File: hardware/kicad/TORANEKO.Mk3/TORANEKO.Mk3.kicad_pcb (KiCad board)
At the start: 2 copper layers, 47.4 x 64 mm, 93 parts, among them IC1 MP6551GQB-P, IC2 MP6551GQB-P, IC3 NCR321PASX, IC4 NCR321PASX, IC5 AS5047P-ATSM, IC6 STM32F411CEU6TR, IC7 AS5047P-ATSM, IC8 NCR321PASX, IC9 NCR321PASX, J1 Conn_01x02_Pin, J2 Conn_01x02_Pin, J3 Conn_01x02_Male, J4 Conn_01x02_Pin, J5 Conn_01x02_Pin, J6 Conn_02x03_Odd_Even, Q1 IRLML6402, Q5 IRLML6344, SW1 SW_Push, U1 LSM6DSRXTR, U2 LXDC55FAAA-203, U3 Encord, U4 Encord_B, U5 Encord, U6 Encord_B, Y1 CSTNE10M0G52Z000R0

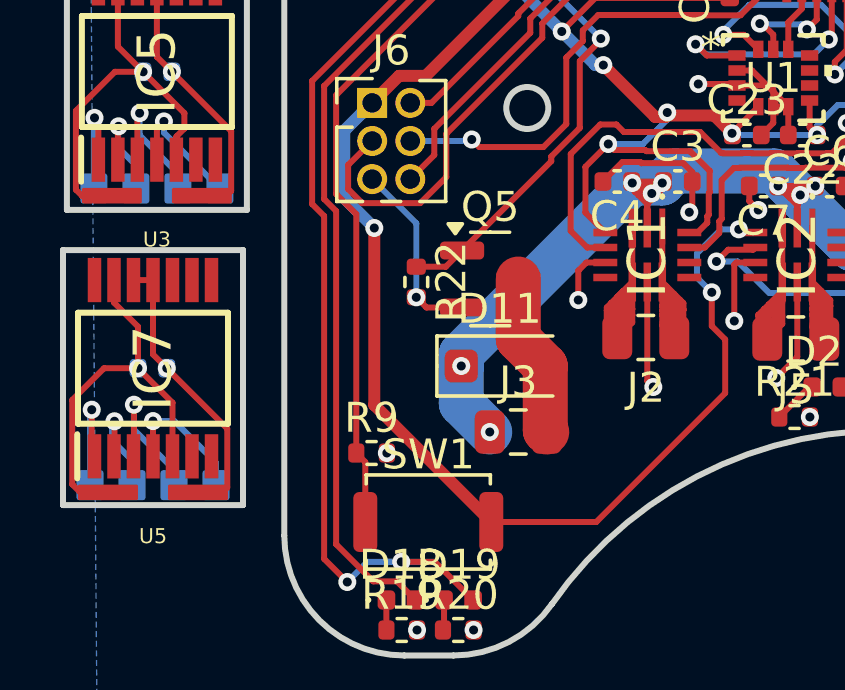
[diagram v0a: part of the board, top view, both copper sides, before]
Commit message: Main PCB check fixes: encoder B edge gap, via spacing, fine-pitch DRC rule
- Move encoder board B outline down 0.05mm so U5 pads are 0.213mm from
  the edge (same as U3; was 0.163mm). Panel regenerated to match.
- Nudge VBAT via at (102.15, 82.65) to (102.1, 82.7): hole gap 0.195 -> 0.27mm
- Add TORANEKO.Mk3.kicad_dru allowing 0.14mm between pads of U1 (LGA-14)
  and IC6 (UFQFPN48), whose footprints are 0.15-0.18mm apart by design

Co-Authored-By: Claude Opus 5.5 <noreply@anthropic.com>
Claude-Session: https://claude.ai/code/session_01Cv6KpZe6NLHWQTjQMUz9Sg
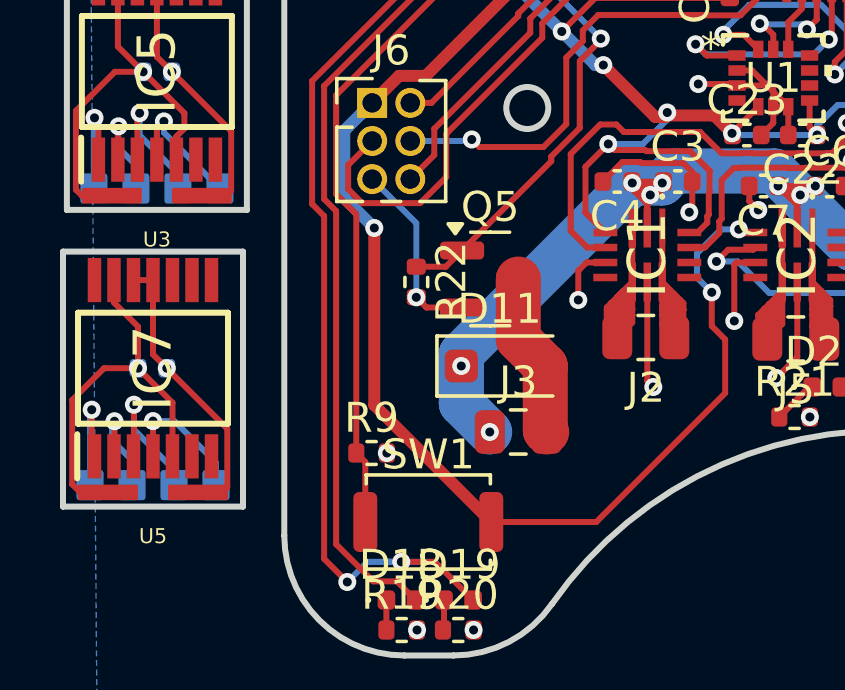
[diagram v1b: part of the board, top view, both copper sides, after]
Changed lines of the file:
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@@
 	)
 	(gr_line
-		(start 82.524 93.0365)
-		(end 88.524 93.0365)
+		(start 82.524 93.0865)
+		(end 88.524 93.0865)
 		(stroke
 			(width 0.2)
@@
 	)
 	(gr_line
-		(start 82.524 84.5365)
-		(end 82.524 93.0365)
+		(start 82.524 84.5865)
+		(end 82.524 93.0865)
 		(stroke
 			(width 0.2)
@@
 	)
 	(gr_line
-		(start 88.524 84.5365)
-		(end 82.524 84.5365)
+		(start 88.524 84.5865)
+		(end 82.524 84.5865)
 		(stroke
 			(width 0.2)
@@
 	)
 	(gr_line
-		(start 88.524 93.0365)
-		(end 88.524 84.5365)
+		(start 88.524 93.0865)
+		(end 88.524 84.5865)
 		(stroke
 			(width 0.2)
@@
 	)
 	(segment
-		(start 102.15 82.65)
+		(start 102.1 82.7)
 		(end 102.5 82.3)
 		(width 0.2)
@@
 	(segment
 		(start 102 82.8)
-		(end 102.15 82.65)
+		(end 102.1 82.7)
 		(width 0.2)
 		(layer "F.Cu")
@@
 	)
 	(via
-		(at 102.15 82.65)
+		(at 102.1 82.7)
 		(size 0.6)
 		(drill 0.3)

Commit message: C3/C6 (VBAT): 10uF -> 1uF 25V 0402 and add to PCBA BOM
No 0402 10uF part rated >=16V exists, and VBAT is 2S LiPo (8.4V max);
C2 (100uF) remains as bulk capacitance.

Co-Authored-By: Claude Opus 5.5 <noreply@anthropic.com>
Claude-Session: https://claude.ai/code/session_01Cv6KpZe6NLHWQTjQMUz9Sg
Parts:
- C3, C6: value 10 -> 1u
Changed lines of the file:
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@@
 			)
 		)
-		(property "Value" "10"
+		(property "Value" "1u"
 			(at 0 1.16 0)
 			(layer "F.Fab")
@@
 			)
 		)
-		(property "Value" "10"
+		(property "Value" "1u"
 			(at 0 1.16 0)
 			(layer "F.Fab")

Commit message: Q1/Q5: IRLML6402/6344 -> AO3401A/AO3400A (JLC Basic parts)
Same SOT-23 pinout (1=G, 2=S, 3=D) and +-12V Vgs rating; removes two
Extended parts from the PCBA order.

Co-Authored-By: Claude Opus 5.5 <noreply@anthropic.com>
Claude-Session: https://claude.ai/code/session_01Cv6KpZe6NLHWQTjQMUz9Sg
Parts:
- Q1: value IRLML6402 -> AO3401A
- Q5: value IRLML6344 -> AO3400A
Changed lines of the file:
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@@
 			)
 		)
-		(property "Value" "IRLML6344"
+		(property "Value" "AO3400A"
 			(at 0 2.4 0)
 			(layer "F.Fab")
@@
 			)
 		)
-		(property "Value" "IRLML6402"
+		(property "Value" "AO3401A"
 			(at 0 2.4 0)
 			(layer "F.Fab")
